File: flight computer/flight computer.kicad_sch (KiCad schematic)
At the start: 32 parts, among them IC1 AT25SF128A-SHB-T, J1 JST, U1 RP2350B, Y1 ABM8G-12.000MHZ-18-D2Y-T

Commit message: General progress on the PCB
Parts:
- C1, C10, C11, C12, C13, C14, C15, C16, C17, C18, C19, C2, C3, C4, C5, C6, C7, C8, C9: footprint Capacitor_SMD:C_0805_2012Metric_Pad1.18x1.45mm_HandSolder -> Capacitor_SMD:C_0603_1608Metric_Pad1.08x0.95mm_HandSolder
- R1, R2, R3, R4, R5, R6: footprint Resistor_SMD:R_0805_2012Metric_Pad1.20x1.40mm_HandSolder -> Resistor_SMD:R_0603_1608Metric_Pad0.98x0.95mm_HandSolder
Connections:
- net pin out 1: now also U1.42 (GPIO33); no longer U1.40 (GPIO32)
- net pin out 2: now also U1.40 (GPIO32); no longer U1.42 (GPIO33)
- net USB_DM renamed USB_DN
- net power controller renamed LED controller
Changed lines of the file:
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@@
 		)
 	)
-	(label "USB_DM"
+	(label "USB_DN"
 		(at 63.5 87.63 0)
 		(effects
@@
 		)
 	)
+	(label "LED controller"
+		(at 80.01 154.94 180)
+		(effects
+			(font
+				(size 1.27 1.27)
+			)
+			(justify right bottom)
+		)
+	)
 	(label "servo PWM 2"
 		(at 130.81 88.9 0)
@@
 		)
 	)
-	(label "power controller"
-		(at 80.01 154.94 180)
-		(effects
-			(font
-				(size 1.27 1.27)
-			)
-			(justify right bottom)
-		)
-	)
 	(label "BNO086 wake"
 		(at 130.81 127 0)
@@
 	)
 	(label "pin out 1"
-		(at 130.81 137.16 0)
+		(at 130.81 139.7 0)
 		(effects
 			(font
@@
 	)
 	(label "pin out 2"
-		(at 130.81 139.7 0)
+		(at 130.81 137.16 0)
 		(effects
 			(font
@@
 			)
 		)
-		(property "Footprint" "Capacitor_SMD:C_0805_2012Metric_Pad1.18x1.45mm_HandSolder"
+		(property "Footprint" "Capacitor_SMD:C_0603_1608Metric_Pad1.08x0.95mm_HandSolder"
 			(at 240.9952 55.88 0)
 			(hide yes)
@@
 			)
 		)
-		(property "Footprint" "Capacitor_SMD:C_0805_2012Metric_Pad1.18x1.45mm_HandSolder"
+		(property "Footprint" "Capacitor_SMD:C_0603_1608Metric_Pad1.08x0.95mm_HandSolder"
 			(at 73.9648 49.53 0)
 			(hide yes)
@@
 			)
 		)
-		(property "Footprint" "Capacitor_SMD:C_0805_2012Metric_Pad1.18x1.45mm_HandSolder"
+		(property "Footprint" "Capacitor_SMD:C_0603_1608Metric_Pad1.08x0.95mm_HandSolder"
 			(at 25.7048 64.77 0)
 			(hide yes)
@@
 			)
 		)
-		(property "Footprint" "Capacitor_SMD:C_0805_2012Metric_Pad1.18x1.45mm_HandSolder"
+		(property "Footprint" "Capacitor_SMD:C_0603_1608Metric_Pad1.08x0.95mm_HandSolder"
 			(at 164.7952 29.21 0)
 			(hide yes)
@@
 			)
 		)
-		(property "Footprint" "Resistor_SMD:R_0805_2012Metric_Pad1.20x1.40mm_HandSolder"
+		(property "Footprint" "Resistor_SMD:R_0603_1608Metric_Pad0.98x0.95mm_HandSolder"
 			(at 48.768 78.74 90)
 			(hide yes)
@@
 			)
 		)
-		(property "Footprint" "Resistor_SMD:R_0805_2012Metric_Pad1.20x1.40mm_HandSolder"
+		(property "Footprint" "Resistor_SMD:R_0603_1608Metric_Pad0.98x0.95mm_HandSolder"
 			(at 76.2 88.392 90)
 			(hide yes)
@@
 			)
 		)
-		(property "Footprint" "Capacitor_SMD:C_0805_2012Metric_Pad1.18x1.45mm_HandSolder"
+		(property "Footprint" "Capacitor_SMD:C_0603_1608Metric_Pad1.08x0.95mm_HandSolder"
 			(at 71.4248 29.21 0)
 			(hide yes)
@@
 			)
 		)
-		(property "Footprint" "Capacitor_SMD:C_0805_2012Metric_Pad1.18x1.45mm_HandSolder"
+		(property "Footprint" "Capacitor_SMD:C_0603_1608Metric_Pad1.08x0.95mm_HandSolder"
 			(at 130.5052 29.21 0)
 			(hide yes)
@@
 			)
 		)
-		(property "Footprint" "Resistor_SMD:R_0805_2012Metric_Pad1.20x1.40mm_HandSolder"
+		(property "Footprint" "Resistor_SMD:R_0603_1608Metric_Pad0.98x0.95mm_HandSolder"
 			(at 59.69 40.132 90)
 			(hide yes)
@@
 			)
 		)
-		(property "Footprint" "Capacitor_SMD:C_0805_2012Metric_Pad1.18x1.45mm_HandSolder"
+		(property "Footprint" "Capacitor_SMD:C_0603_1608Metric_Pad1.08x0.95mm_HandSolder"
 			(at 176.2252 29.21 0)
 			(hide yes)
@@
 			)
 		)
-		(property "Footprint" "Capacitor_SMD:C_0805_2012Metric_Pad1.18x1.45mm_HandSolder"
+		(property "Footprint" "Capacitor_SMD:C_0603_1608Metric_Pad1.08x0.95mm_HandSolder"
 			(at 187.6552 29.21 0)
 			(hide yes)
@@
 			)
 		)
-		(property "Footprint" "Resistor_SMD:R_0805_2012Metric_Pad1.20x1.40mm_HandSolder"
+		(property "Footprint" "Resistor_SMD:R_0603_1608Metric_Pad0.98x0.95mm_HandSolder"
 			(at 190.5 98.552 90)
 			(hide yes)
@@
 			)
 		)
-		(property "Footprint" "Capacitor_SMD:C_0805_2012Metric_Pad1.18x1.45mm_HandSolder"
+		(property "Footprint" "Capacitor_SMD:C_0603_1608Metric_Pad1.08x0.95mm_HandSolder"
 			(at 94.2848 29.21 0)
 			(hide yes)
@@
 			)
 		)
-		(property "Footprint" "Resistor_SMD:R_0805_2012Metric_Pad1.20x1.40mm_HandSolder"
+		(property "Footprint" "Resistor_SMD:R_0603_1608Metric_Pad0.98x0.95mm_HandSolder"
 			(at 76.2 85.852 90)
 			(hide yes)
@@
 			)
 		)
-		(property "Footprint" "Capacitor_SMD:C_0805_2012Metric_Pad1.18x1.45mm_HandSolder"
+		(property "Footprint" "Capacitor_SMD:C_0603_1608Metric_Pad1.08x0.95mm_HandSolder"
 			(at 209.55 101.2952 0)
 			(hide yes)
@@
 			)
 		)
-		(property "Footprint" "Capacitor_SMD:C_0805_2012Metric_Pad1.18x1.45mm_HandSolder"
+		(property "Footprint" "Capacitor_SMD:C_0603_1608Metric_Pad1.08x0.95mm_HandSolder"
 			(at 199.0852 29.21 0)
 			(hide yes)
@@
 			)
 		)
-		(property "Footprint" "Capacitor_SMD:C_0805_2012Metric_Pad1.18x1.45mm_HandSolder"
+		(property "Footprint" "Capacitor_SMD:C_0603_1608Metric_Pad1.08x0.95mm_HandSolder"
 			(at 229.5652 55.88 0)
 			(hide yes)
@@
 			)
 		)
-		(property "Footprint" "Capacitor_SMD:C_0805_2012Metric_Pad1.18x1.45mm_HandSolder"
+		(property "Footprint" "Capacitor_SMD:C_0603_1608Metric_Pad1.08x0.95mm_HandSolder"
 			(at 119.0752 29.21 0)
 			(hide yes)
@@
 			)
 		)
-		(property "Footprint" "Capacitor_SMD:C_0805_2012Metric_Pad1.18x1.45mm_HandSolder"
+		(property "Footprint" "Capacitor_SMD:C_0603_1608Metric_Pad1.08x0.95mm_HandSolder"
 			(at 153.3652 29.21 0)
 			(hide yes)
@@
 			)
 		)
-		(property "Footprint" "Capacitor_SMD:C_0805_2012Metric_Pad1.18x1.45mm_HandSolder"
+		(property "Footprint" "Capacitor_SMD:C_0603_1608Metric_Pad1.08x0.95mm_HandSolder"
 			(at 210.5152 29.21 0)
 			(hide yes)
@@
 			)
 		)
-		(property "Footprint" "Capacitor_SMD:C_0805_2012Metric_Pad1.18x1.45mm_HandSolder"
+		(property "Footprint" "Capacitor_SMD:C_0603_1608Metric_Pad1.08x0.95mm_HandSolder"
 			(at 209.55 91.1352 0)
 			(hide yes)
@@
 			)
 		)
-		(property "Footprint" "Capacitor_SMD:C_0805_2012Metric_Pad1.18x1.45mm_HandSolder"
+		(property "Footprint" "Capacitor_SMD:C_0603_1608Metric_Pad1.08x0.95mm_HandSolder"
 			(at 141.9352 29.21 0)
 			(hide yes)
@@
 			)
 		)
-		(property "Footprint" "Resistor_SMD:R_0805_2012Metric_Pad1.20x1.40mm_HandSolder"
+		(property "Footprint" "Resistor_SMD:R_0603_1608Metric_Pad0.98x0.95mm_HandSolder"
 			(at 50.8 97.282 90)
 			(hide yes)
@@
 			)
 		)
-		(property "Footprint" "Capacitor_SMD:C_0805_2012Metric_Pad1.18x1.45mm_HandSolder"
+		(property "Footprint" "Capacitor_SMD:C_0603_1608Metric_Pad1.08x0.95mm_HandSolder"
 			(at 37.1348 64.77 0)
 			(hide yes)
@@
 			)
 		)
-		(property "Footprint" "Capacitor_SMD:C_0805_2012Metric_Pad1.18x1.45mm_HandSolder"
+		(property "Footprint" "Capacitor_SMD:C_0603_1608Metric_Pad1.08x0.95mm_HandSolder"
 			(at 82.8548 29.21 0)
 			(hide yes)

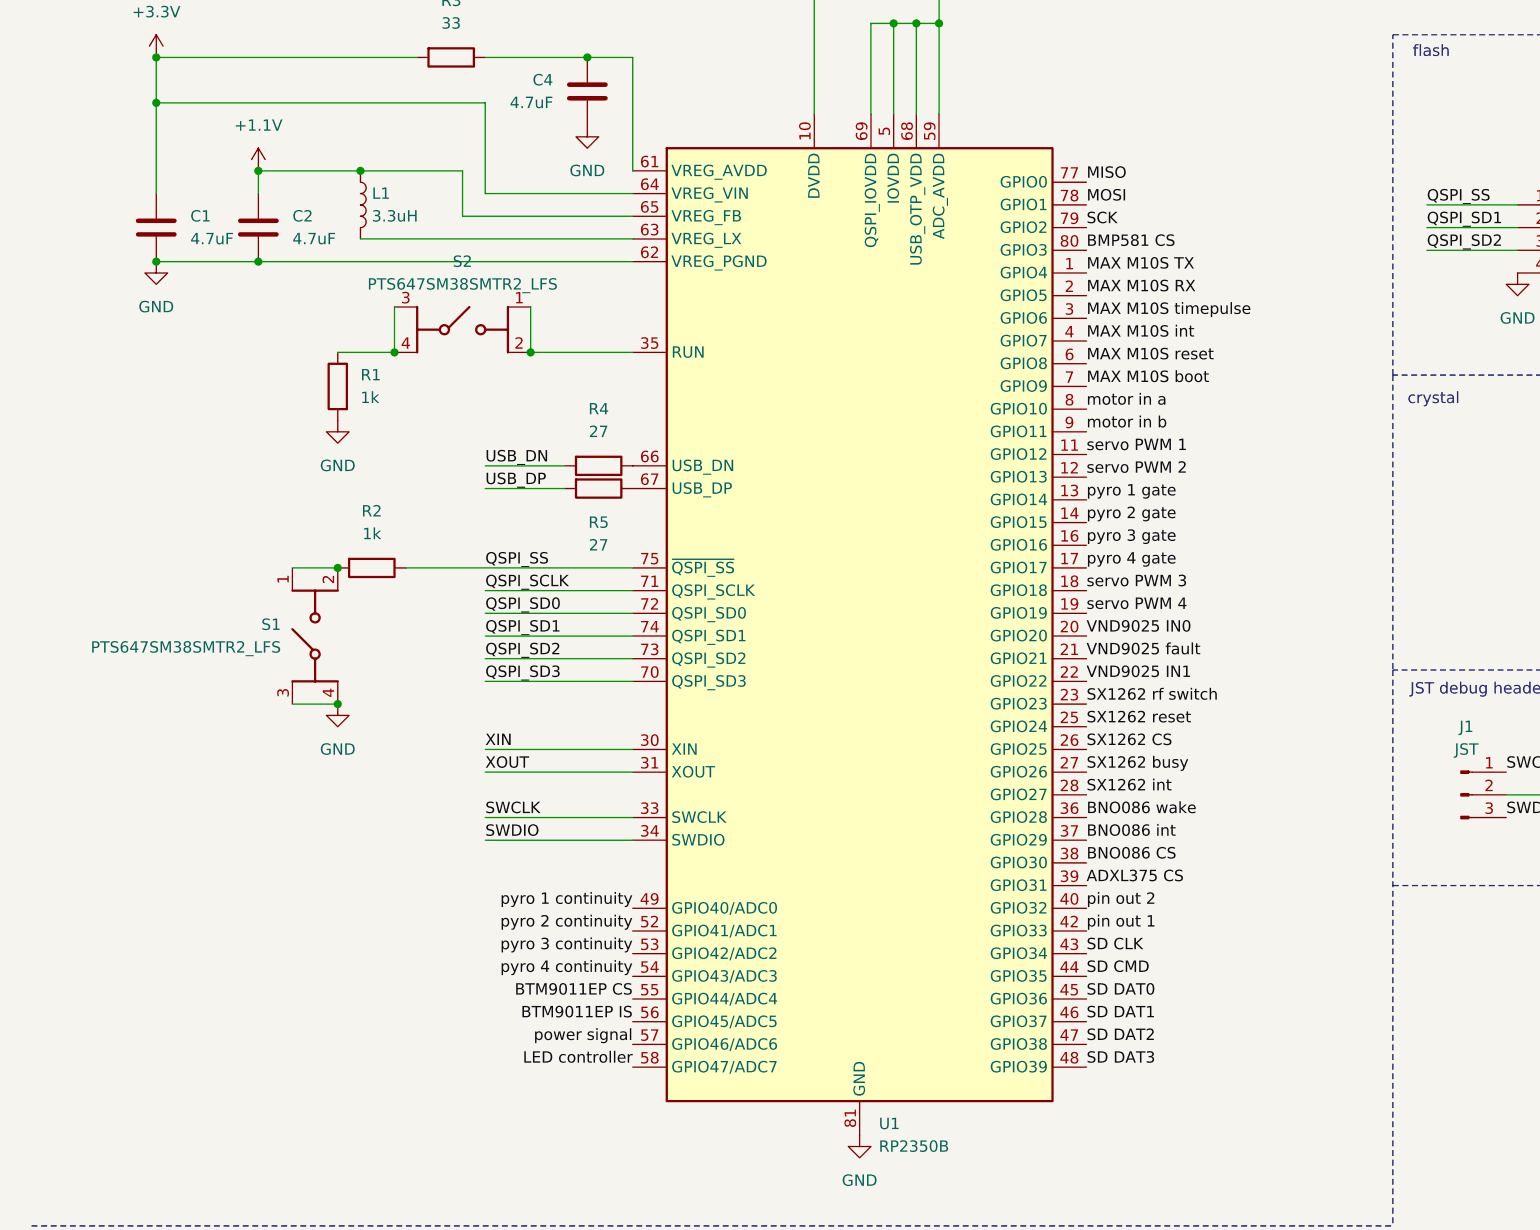
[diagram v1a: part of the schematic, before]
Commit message: Tried a more effective layout
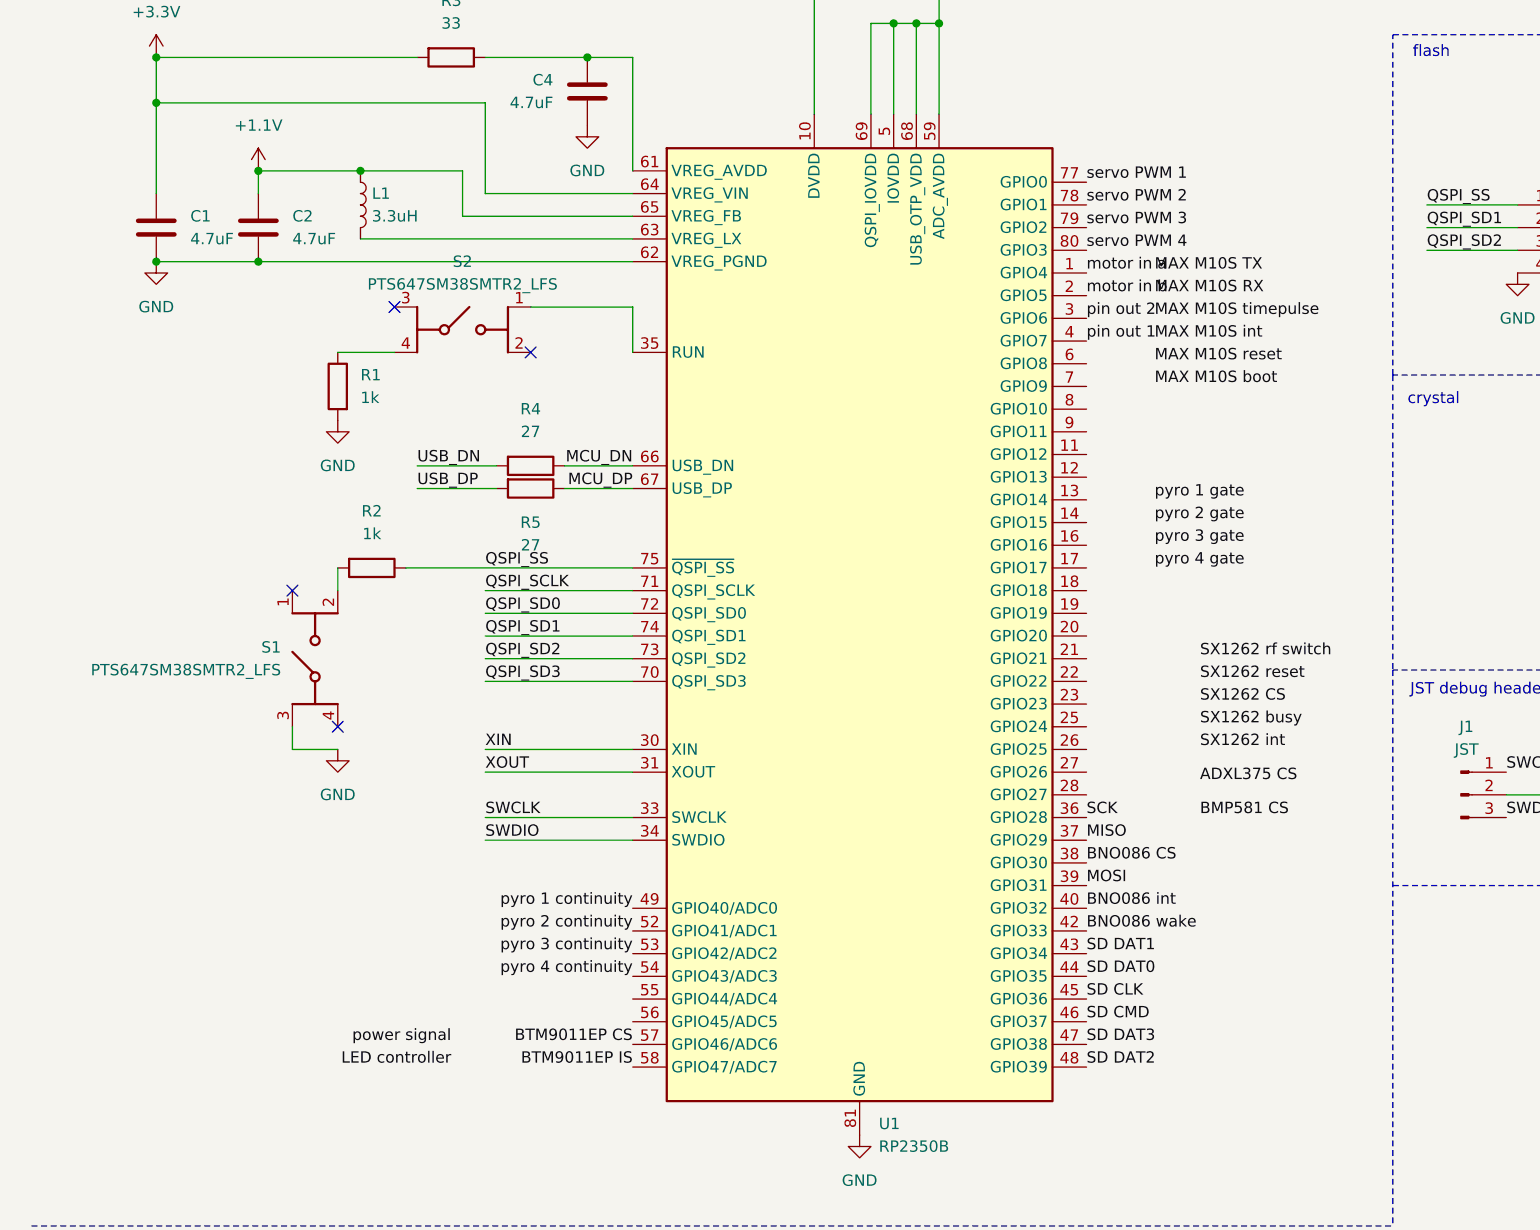
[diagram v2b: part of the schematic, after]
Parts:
- U1: footprint Package_DFN_QFN:QFN-80-1EP_10x10mm_P0.4mm_EP3.4x3.4mm -> Package_DFN_QFN:QFN-80-1EP_10x10mm_P0.4mm_EP3.4x3.4mm_ThermalVias
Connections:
- net ADXL375 CS: no longer U1.39 (GPIO31)
- net BMP581 CS: no longer U1.80 (GPIO3)
- net BNO086 int: now also U1.40 (GPIO32); no longer U1.37 (GPIO29)
- net BNO086 wake: now also U1.42 (GPIO33); no longer U1.36 (GPIO28)
- net BTM9011EP CS: now also U1.57 (GPIO46/ADC6); no longer U1.55 (GPIO44/ADC4)
- net BTM9011EP IS: now also U1.58 (GPIO47/ADC7); no longer U1.56 (GPIO45/ADC5)
- net GND: no longer S1.4 (COM_2)
- net LED controller: no longer U1.58 (GPIO47/ADC7)
- net MAX M10S RX: no longer U1.2 (GPIO5)
- net MAX M10S TX: no longer U1.1 (GPIO4)
- net MAX M10S boot: no longer U1.7 (GPIO9)
- net MAX M10S int: no longer U1.4 (GPIO7)
- net MAX M10S reset: no longer U1.6 (GPIO8)
- net MAX M10S timepulse: no longer U1.3 (GPIO6)
- net MISO: now also U1.37 (GPIO29); no longer U1.77 (GPIO0)
- net MOSI: now also U1.39 (GPIO31); no longer U1.78 (GPIO1)
- net SCK: now also U1.36 (GPIO28); no longer U1.79 (GPIO2)
- net SD CLK: now also U1.45 (GPIO36); no longer U1.43 (GPIO34)
- net SD CMD: now also U1.46 (GPIO37); no longer U1.44 (GPIO35)
- net SD DAT0: now also U1.44 (GPIO35); no longer U1.45 (GPIO36)
- net SD DAT1: now also U1.43 (GPIO34); no longer U1.46 (GPIO37)
- net SD DAT2: now also U1.48 (GPIO39); no longer U1.47 (GPIO38)
- net SD DAT3: now also U1.47 (GPIO38); no longer U1.48 (GPIO39)
- net SX1262 CS: no longer U1.26 (GPIO25)
- net SX1262 busy: no longer U1.27 (GPIO26)
- net SX1262 int: no longer U1.28 (GPIO27)
- net SX1262 reset: no longer U1.25 (GPIO24)
- net SX1262 rf switch: no longer U1.23 (GPIO23)
- net motor in a: now also U1.1 (GPIO4); no longer U1.8 (GPIO10)
- net motor in b: now also U1.2 (GPIO5); no longer U1.9 (GPIO11)
- net pin out 1: now also U1.4 (GPIO7); no longer U1.42 (GPIO33)
- net pin out 2: now also U1.3 (GPIO6); no longer U1.40 (GPIO32)
- net power signal: no longer U1.57 (GPIO46/ADC6)
- net pyro 1 gate: no longer U1.13 (GPIO14)
- net pyro 2 gate: no longer U1.14 (GPIO15)
- net pyro 3 gate: no longer U1.16 (GPIO16)
- net pyro 4 gate: no longer U1.17 (GPIO17)
- net servo PWM 1: now also U1.77 (GPIO0); no longer U1.11 (GPIO12)
- net servo PWM 2: now also U1.78 (GPIO1); no longer U1.12 (GPIO13)
- net servo PWM 3: now also U1.79 (GPIO2); no longer U1.18 (GPIO18)
- net servo PWM 4: now also U1.80 (GPIO3); no longer U1.19 (GPIO19)
- net at R1.1, S2.4 (COM_2): no longer S2.3 (COM_1)
- net MCU_DP: now reaches R5.1, U1.67 (USB_DP)
- net at S2.1 (NO_1), U1.35 (RUN): no longer S2.2 (NO_2)
- net MCU_DN: now reaches R4.1, U1.66 (USB_DN)
- net at R2.2, S1.2 (NO_2): no longer S1.1 (NO_1)
- net VND9025 IN0: no longer names the net of U1.20 (GPIO20)
- net VND9025 IN1: no longer names the net of U1.22 (GPIO22)
- net VND9025 fault: no longer names the net of U1.21 (GPIO21)
- no-connect marks 0 -> 4
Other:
- moved on the sheet: R4, R5, S1

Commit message: Power rail optimisations
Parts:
- removed R1, R2: 1k, Resistor_SMD:R_0603_1608Metric_Pad0.98x0.95mm_HandSolder, symbol Device:R
- added R11, R7: 1k, Resistor_SMD:R_0603_1608Metric_Pad0.98x0.95mm_HandSolder, symbol Device:R
- U1: footprint Package_DFN_QFN:QFN-80-1EP_10x10mm_P0.4mm_EP3.4x3.4mm_ThermalVias -> Package_DFN_QFN:QFN-80-1EP_10x10mm_P0.4mm_EP3.4x3.4mm
- Y1: value ABM8G-12.000MHZ-18-D2Y-T -> ABM8-272-T3; footprint Snapeda:CRYSTAL_ABM8G_ABR-L -> Samacsys:ABM8272T3
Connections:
- net BNO086 CS: no longer U1.38 (GPIO30)
- net BNO086 int: no longer U1.40 (GPIO32)
- net BNO086 wake: no longer U1.42 (GPIO33)
- net BTM9011EP CS: no longer U1.57 (GPIO46/ADC6)
- net BTM9011EP IS: no longer U1.58 (GPIO47/ADC7)
- net GND: now also S2.4 (COM_2), R7.1; no longer S1.3 (COM_1)
- net MISO: no longer U1.37 (GPIO29)
- net MOSI: no longer U1.39 (GPIO31)
- net QSPI_SS: now also S1.2 (NO_2)
- net SCK: no longer U1.36 (GPIO28)
- net SD CLK: no longer U1.45 (GPIO36)
- net SD CMD: no longer U1.46 (GPIO37)
- net SD DAT0: no longer U1.44 (GPIO35)
- net SD DAT1: no longer U1.43 (GPIO34)
- net SD DAT2: no longer U1.48 (GPIO39)
- net SD DAT3: no longer U1.47 (GPIO38)
- net motor in a: no longer U1.1 (GPIO4)
- net motor in b: no longer U1.2 (GPIO5)
- net pin out 1: no longer U1.4 (GPIO7)
- net pin out 2: no longer U1.3 (GPIO6)
- net pyro 1 continuity: no longer U1.49 (GPIO40/ADC0)
- net pyro 2 continuity: no longer U1.52 (GPIO41/ADC1)
- net pyro 3 continuity: no longer U1.53 (GPIO42/ADC2)
- net pyro 4 continuity: no longer U1.54 (GPIO43/ADC3)
- net servo PWM 1: no longer U1.77 (GPIO0)
- net servo PWM 2: no longer U1.78 (GPIO1)
- net servo PWM 3: no longer U1.79 (GPIO2)
- net servo PWM 4: no longer U1.80 (GPIO3)
- net at U1.35 (RUN): now also R11.1; no longer S2.1 (NO_1)
- new net: R11.2, S2.1 (NO_1)
- new net: R7.2, S1.3 (COM_1)
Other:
- moved on the sheet: S1
